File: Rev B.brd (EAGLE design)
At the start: 100.3 x 61 mm, 39 parts

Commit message: Made some changes to the backlight circuit
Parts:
- removed JP_BKL: (no value), pinhead:2X02
- added PRGHDR: (no value), pinhead:1X03
- added Q1: BC817-25LT1SMD, transistor-npn:SOT23-BEC
- added R9: 10kΩ, rcl:R0805
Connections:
- removed net N$11: JP_BKL.3, LCD.15
- new net BKL_CTRL: MCU.4, R9.1
- new net N$16: Q1.B, R9.2
- new net RST: MCU.16, PRGHDR.3, R7.2
- new net TEST: MCU.17, PRGHDR.2
- net +5V: now also LCD.15; no longer JP_BKL.4
- net GND: now also PRGHDR.1, Q1.E; no longer LCD.16
- net N$9: now also LCD.16, Q1.C; no longer MCU.16, R7.2
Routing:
- net BKL_CTRL: track 0.00 -> 52.1 mm, vias 0 -> 1
- net N$11: track 43.9 -> 0.00 mm, vias 1 -> 0
- net RST: track 0.00 -> 43.2 mm
- net TEST: track 0.00 -> 22.4 mm, vias 0 -> 1
- net N$9: track 19.3 -> 38.2 mm, vias 0 -> 1
- net +5V: track 104.1 -> 89.9 mm, vias 5 -> 4
- net N$16: track 0.00 -> 3.64 mm
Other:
- board text removed: "Backlight"
- board text removed: "OFF"

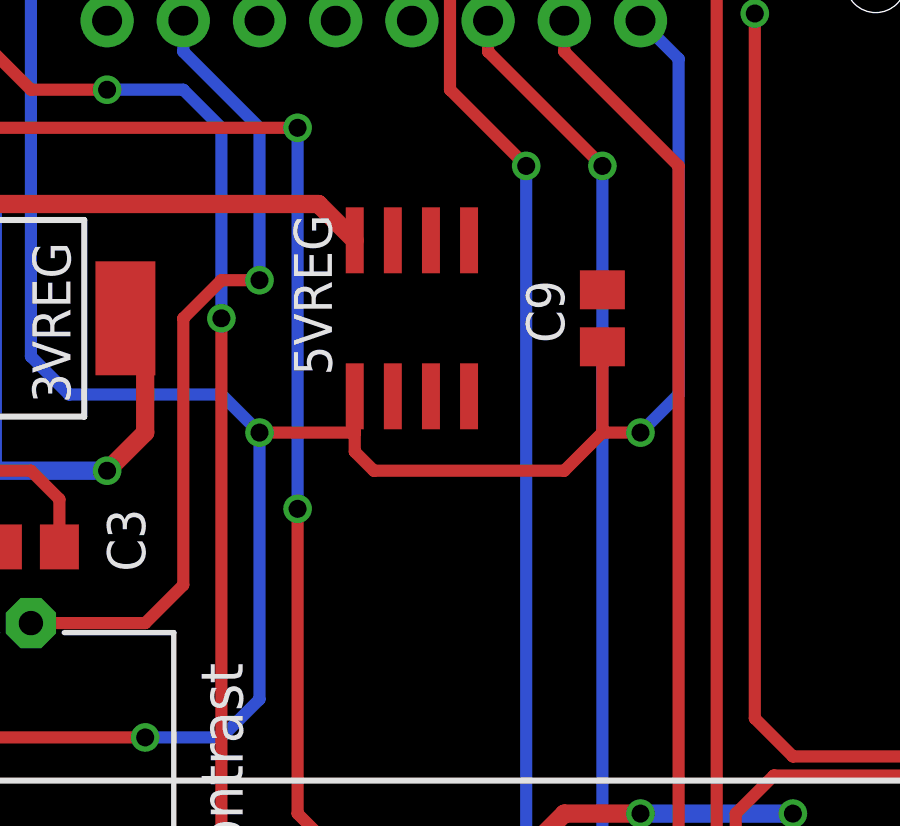
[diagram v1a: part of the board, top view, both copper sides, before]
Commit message: Changed the 5V regulators
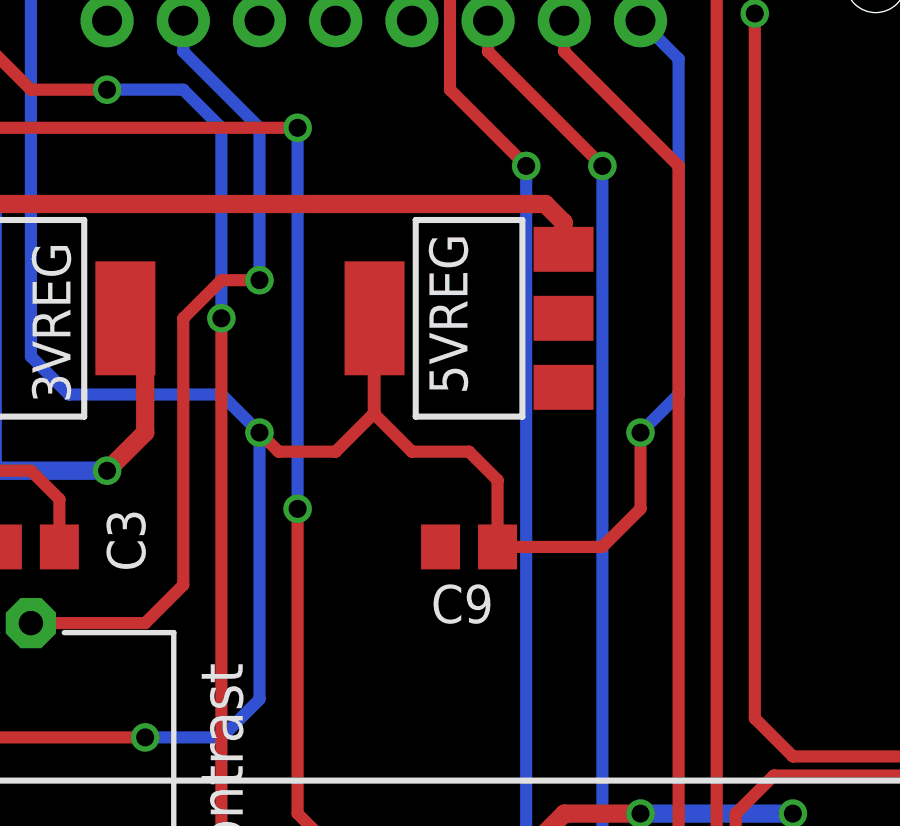
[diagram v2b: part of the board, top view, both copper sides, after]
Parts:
- 5VREG: value 78L05SMD -> LD117AS50TR; device linear:SO08 -> v-reg:SOT223
- moved C9 8.82 mm to (31.1, 38.1), turned to 0 degrees
- moved 5VREG 1.90 mm to (31.1, 45.7), turned to 90 degrees
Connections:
- net +5V: now also 5VREG.4; no longer 5VREG.1
- net GND: now also 5VREG.1; no longer 5VREG.2, 5VREG.3, 5VREG.6, 5VREG.7
- net N$6: now also 5VREG.3; no longer 5VREG.8
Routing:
- net +5V: track 89.9 -> 97.8 mm
- net N$6: track 55.2 -> 62.8 mm
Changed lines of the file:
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@@
 </element>
 <element name="VO" library="bourns" package="3386G" value="10kΩ" x="16.51" y="30.48"/>
-<element name="5VREG" library="linear" package="SO08" value="78L05SMD" x="29.21" y="45.72"/>
-<element name="C9" library="rcl" package="C0805" value="0.1uF" x="35.56" y="45.72" smashed="yes" rot="R270">
-<attribute name="NAME" x="33.02" y="46.99" size="1.27" layer="25" rot="R270"/>
-<attribute name="VALUE" x="33.02" y="46.99" size="1.27" layer="27" rot="R270"/>
+<element name="C9" library="rcl" package="C0805" value="0.1uF" x="31.115" y="38.1" smashed="yes">
+<attribute name="NAME" x="29.845" y="35.56" size="1.27" layer="25"/>
+<attribute name="VALUE" x="29.845" y="35.56" size="1.27" layer="27"/>
 </element>
 <element name="PWR_IN" library="SparkFun-Connectors" package="JST-2-PTH" value="M02JST-PTH-2" x="93.98" y="24.13" rot="R270"/>
@@
 <element name="Q1" library="transistor-npn" package="SOT23-BEC" value="BC817-25LT1SMD" x="50.165" y="31.115" rot="R90"/>
 <element name="R9" library="rcl" package="R0805" value="10kΩ" x="50.165" y="26.035" rot="R90"/>
+<element name="5VREG" library="v-reg" package="SOT223" value="LD117AS50TR" x="31.115" y="45.72" rot="R90"/>
 </elements>
 <signals>
@@
 <contactref element="RE1" pad="SW+"/>
 <contactref element="VO" pad="3"/>
-<contactref element="5VREG" pad="2"/>
-<contactref element="5VREG" pad="7"/>
-<contactref element="5VREG" pad="6"/>
-<contactref element="5VREG" pad="3"/>
 <contactref element="C9" pad="1"/>
 <contactref element="PWR_IN" pad="1"/>
@@
 <contactref element="PRGHDR" pad="1"/>
 <contactref element="Q1" pad="E"/>
+<contactref element="5VREG" pad="1"/>
 <wire x1="90.17" y1="24.13" x2="93.98" y2="25.13" width="0" layer="19" extent="1-1"/>
 <wire x1="90.17" y1="29.21" x2="90.17" y2="24.13" width="0" layer="19" extent="1-1"/>
@@
 <wire x1="48.26" y1="18.1" x2="58.42" y2="6.35" width="0" layer="19" extent="1-1"/>
 <wire x1="43.18" y1="20" x2="48.26" y2="18.1" width="0" layer="19" extent="1-1"/>
-<wire x1="19.05" y1="25.4" x2="43.18" y2="20" width="0" layer="19" extent="1-1"/>
+<wire x1="51.265" y1="32.065" x2="48.26" y2="18.1" width="0" layer="19" extent="1-1"/>
+<wire x1="30.165" y1="38.1" x2="51.265" y2="32.065" width="0" layer="19" extent="1-1"/>
+<wire x1="24.13" y1="55.64" x2="30.165" y2="38.1" width="0" layer="19" extent="1-1"/>
+<wire x1="19.05" y1="55.64" x2="24.13" y2="55.64" width="0" layer="19" extent="1-1"/>
+<wire x1="13.36" y1="48.02" x2="19.05" y2="55.64" width="0" layer="19" extent="1-1"/>
+<wire x1="3.81" y1="45.59" x2="13.36" y2="48.02" width="0" layer="19" extent="1-1"/>
+<wire x1="15.56" y1="38.1" x2="13.36" y2="48.02" width="0" layer="19" extent="1-1"/>
+<wire x1="11.11" y1="38.1" x2="15.56" y2="38.1" width="0" layer="19" extent="1-1"/>
+<wire x1="6.35" y1="56.15" x2="13.36" y2="48.02" width="0" layer="19" extent="1-1"/>
+<wire x1="3.81" y1="27.94" x2="11.11" y2="38.1" width="0" layer="19" extent="1-1"/>
+<wire x1="19.05" y1="25.4" x2="15.56" y2="38.1" width="0" layer="19" extent="1-1"/>
 <wire x1="15.235" y1="20.32" x2="19.05" y2="25.4" width="0" layer="19" extent="1-1"/>
 <wire x1="10.16" y1="13.02" x2="15.235" y2="20.32" width="0" layer="19" extent="1-1"/>
 <wire x1="3.81" y1="11.43" x2="10.16" y2="13.02" width="0" layer="19" extent="1-1"/>
-<wire x1="15.56" y1="38.1" x2="19.05" y2="25.4" width="0" layer="19" extent="1-1"/>
-<wire x1="11.11" y1="38.1" x2="15.56" y2="38.1" width="0" layer="19" extent="1-1"/>
-<wire x1="13.36" y1="48.02" x2="15.56" y2="38.1" width="0" layer="19" extent="1-1"/>
-<wire x1="19.05" y1="55.64" x2="13.36" y2="48.02" width="0" layer="19" extent="1-1"/>
-<wire x1="24.13" y1="55.64" x2="19.05" y2="55.64" width="0" layer="19" extent="1-1"/>
-<wire x1="28.575" y1="48.32" x2="24.13" y2="55.64" width="0" layer="19" extent="1-1"/>
-<wire x1="29.845" y1="48.32" x2="28.575" y2="48.32" width="0" layer="19" extent="1-1"/>
-<wire x1="28.575" y1="43.12" x2="28.575" y2="48.32" width="0" layer="19" extent="1-1"/>
-<wire x1="29.845" y1="43.12" x2="28.575" y2="43.12" width="0" layer="19" extent="1-1"/>
-<wire x1="35.56" y1="46.67" x2="29.845" y2="48.32" width="0" layer="19" extent="1-1"/>
-<wire x1="3.81" y1="45.59" x2="13.36" y2="48.02" width="0" layer="19" extent="1-1"/>
-<wire x1="6.35" y1="56.15" x2="13.36" y2="48.02" width="0" layer="19" extent="1-1"/>
-<wire x1="3.81" y1="27.94" x2="11.11" y2="38.1" width="0" layer="19" extent="1-1"/>
-<wire x1="51.265" y1="32.065" x2="3.81" y2="11.43" width="0" layer="19" extent="1-1"/>
+<wire x1="34.265" y1="43.42" x2="3.81" y2="11.43" width="0" layer="19" extent="1-1"/>
 </signal>
 <signal name="VCC">
@@
 <wire x1="11.43" y1="43.18" x2="13.12" y2="43.18" width="0.6096" layer="1"/>
 <wire x1="13.12" y1="43.18" x2="13.36" y2="43.42" width="0.6096" layer="1"/>
-<contactref element="5VREG" pad="8"/>
 <wire x1="9.16" y1="46.72" x2="9.16" y2="46.99" width="0.6096" layer="1"/>
 <wire x1="9.16" y1="46.99" x2="9.16" y2="48.53" width="0.6096" layer="1"/>
 <wire x1="9.16" y1="48.53" x2="10.16" y2="49.53" width="0.6096" layer="1"/>
 <wire x1="10.16" y1="49.53" x2="26.095" y2="49.53" width="0.6096" layer="1"/>
-<wire x1="26.095" y1="49.53" x2="27.305" y2="48.32" width="0.6096" layer="1"/>
 <wire x1="6.35" y1="58.15" x2="4.81" y2="58.15" width="0.6096" layer="16"/>
 <wire x1="4.81" y1="58.15" x2="2.54" y2="55.88" width="0.6096" layer="16"/>
@@
 <wire x1="9.16" y1="46.99" x2="6.985" y2="46.99" width="0.6096" layer="1"/>
 <via x="6.985" y="46.99" extent="1-16" drill="0.6"/>
+<contactref element="5VREG" pad="3"/>
+<wire x1="34.265" y1="48.02" x2="34.265" y2="48.92" width="0.6096" layer="1"/>
+<wire x1="34.265" y1="48.92" x2="33.655" y2="49.53" width="0.6096" layer="1"/>
+<wire x1="33.655" y1="49.53" x2="26.095" y2="49.53" width="0.6096" layer="1"/>
 </signal>
 <signal name="N$7">
@@
 </signal>
 <signal name="+5V">
-<contactref element="5VREG" pad="1"/>
 <contactref element="VO" pad="1"/>
 <contactref element="LCD" pad="2"/>
 <contactref element="C9" pad="2"/>
-<wire x1="27.94" y1="40.64" x2="27.305" y2="41.275" width="0.4064" layer="1"/>
-<wire x1="27.305" y1="41.275" x2="27.305" y2="41.91" width="0.4064" layer="1"/>
-<wire x1="27.305" y1="41.91" x2="27.305" y2="43.12" width="0.4064" layer="1"/>
-<wire x1="27.94" y1="40.64" x2="34.29" y2="40.64" width="0.4064" layer="1"/>
-<wire x1="34.29" y1="40.64" x2="35.56" y2="41.91" width="0.4064" layer="1"/>
-<wire x1="35.56" y1="41.91" x2="35.56" y2="44.77" width="0.4064" layer="1"/>
 <wire x1="19.05" y1="58.18" x2="17.54" y2="58.18" width="0.4064" layer="1"/>
 <wire x1="17.54" y1="58.18" x2="16.51" y2="57.15" width="0.4064" layer="1"/>
@@
 <wire x1="22.86" y1="43.18" x2="24.13" y2="41.91" width="0.4064" layer="16"/>
 <via x="24.13" y="41.91" extent="1-16" drill="0.6"/>
-<wire x1="24.13" y1="41.91" x2="27.305" y2="41.91" width="0.4064" layer="1"/>
 <via x="36.83" y="41.91" extent="1-16" drill="0.6"/>
-<wire x1="36.83" y1="41.91" x2="35.56" y2="41.91" width="0.4064" layer="1"/>
 <wire x1="13.97" y1="25.4" x2="13.97" y2="30.48" width="0.4064" layer="1"/>
 <wire x1="13.97" y1="30.48" x2="15.24" y2="31.75" width="0.4064" layer="1"/>
@@
 <wire x1="38.1" y1="43.18" x2="38.1" y2="54.37" width="0.4064" layer="16"/>
 <wire x1="38.1" y1="54.37" x2="36.83" y2="55.64" width="0.4064" layer="16"/>
+<contactref element="5VREG" pad="4"/>
+<wire x1="36.83" y1="41.91" x2="36.83" y2="39.37" width="0.4064" layer="1"/>
+<wire x1="36.83" y1="39.37" x2="35.56" y2="38.1" width="0.4064" layer="1"/>
+<wire x1="35.56" y1="38.1" x2="32.065" y2="38.1" width="0.4064" layer="1"/>
+<wire x1="32.065" y1="38.1" x2="32.065" y2="40.325" width="0.4064" layer="1"/>
+<wire x1="32.065" y1="40.325" x2="31.115" y2="41.275" width="0.4064" layer="1"/>
+<wire x1="31.115" y1="41.275" x2="29.21" y2="41.275" width="0.4064" layer="1"/>
+<wire x1="29.21" y1="41.275" x2="27.94" y2="42.545" width="0.4064" layer="1"/>
+<wire x1="27.94" y1="42.545" x2="27.94" y2="45.695" width="0.4064" layer="1"/>
+<wire x1="27.94" y1="45.695" x2="27.965" y2="45.72" width="0.4064" layer="1"/>
+<wire x1="27.965" y1="45.72" x2="27.965" y2="42.57" width="0.4064" layer="1"/>
+<wire x1="27.965" y1="42.57" x2="26.67" y2="41.275" width="0.4064" layer="1"/>
+<wire x1="26.67" y1="41.275" x2="24.765" y2="41.275" width="0.4064" layer="1"/>
+<wire x1="24.765" y1="41.275" x2="24.13" y2="41.91" width="0.4064" layer="1"/>
 </signal>
 <signal name="N$2">

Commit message: Final design
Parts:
- removed VO: 10kΩ, bourns:3386G
- added R10: TRIMPOT-2, SparkFun-Electromechanical:TRIMPOT_TC33
- moved 5V 1.27 mm to (7.62, 21.6)
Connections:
- net +5V: now also R10.1; no longer VO.1
- net GND: now also R10.3; no longer VO.3
- net N$10: now also R10.2; no longer VO.2
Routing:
- net N$10: track 27.3 -> 33.6 mm
- net +5V: track 97.8 -> 103.7 mm
- net BKL_CTRL: track 52.1 -> 53.1 mm
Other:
- board text added: "Rev B"
- board text removed: "Contrast"
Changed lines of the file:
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@@
 <text x="3.81" y="40.64" size="1.6764" layer="21" font="vector" align="center">ON</text>
 <text x="74.93" y="38.1" size="1.6764" layer="21" font="vector" align="center">MOSFET</text>
-<text x="22.86" y="30.48" size="1.4224" layer="21" rot="R90" align="center">Contrast</text>
 <text x="96.52" y="29.21" size="1.9304" layer="21" align="center">Input</text>
 <text x="24.13" y="7.62" size="3.81" layer="21" align="center">miniLoad</text>
@@
 <rectangle x1="53.34" y1="59.69" x2="96.52" y2="60.96" layer="41"/>
 <text x="3.81" y="52.705" size="1.778" layer="21" align="center">PWR</text>
-<wire x1="2.54" y1="8.89" x2="5.08" y2="8.89" width="0.4064" layer="21"/>
-<wire x1="5.08" y1="8.89" x2="5.08" y2="10.16" width="0.4064" layer="21"/>
-<wire x1="2.54" y1="8.89" x2="2.54" y2="10.16" width="0.4064" layer="21"/>
+<wire x1="5.08" y1="10.16" x2="6.35" y2="10.16" width="0.4064" layer="21"/>
+<wire x1="6.35" y1="10.16" x2="6.35" y2="12.7" width="0.4064" layer="21"/>
+<wire x1="6.35" y1="12.7" x2="5.08" y2="12.7" width="0.4064" layer="21"/>
+<wire x1="2.54" y1="18.415" x2="5.08" y2="18.415" width="0.4064" layer="21"/>
+<wire x1="2.54" y1="19.05" x2="5.08" y2="19.05" width="0.4064" layer="21"/>
+<text x="5.08" y="1.905" size="1.27" layer="21" align="center">Rev B</text>
 </plain>
 <attributes>
@@
 <attribute name="VALUE" x="80.01" y="17.145" size="1.27" layer="27" rot="R270"/>
 </element>
-<element name="VO" library="bourns" package="3386G" value="10kΩ" x="16.51" y="30.48"/>
 <element name="C9" library="rcl" package="C0805" value="0.1uF" x="31.115" y="38.1" smashed="yes">
 <attribute name="NAME" x="29.845" y="35.56" size="1.27" layer="25"/>
@@
 <attribute name="TP_SIGNAL_NAME" value="" x="7.62" y="15.24" size="1.27" layer="27" rot="R90" display="off"/>
 </element>
-<element name="5V" library="testpad" package="TP10SQ" value="PTR1TP10SQ" x="7.62" y="22.86" rot="R90">
-<attribute name="TP_SIGNAL_NAME" value="" x="7.62" y="22.86" size="1.27" layer="27" rot="R90" display="off"/>
+<element name="5V" library="testpad" package="TP10SQ" value="PTR1TP10SQ" x="7.62" y="21.59" rot="R90">
+<attribute name="TP_SIGNAL_NAME" value="" x="7.62" y="21.59" size="1.27" layer="27" rot="R90" display="off"/>
 </element>
 <element name="GND" library="testpad" package="TP10SQ" value="PTR1TP10SQ" x="3.81" y="27.94" rot="R90">
@@
 <element name="R9" library="rcl" package="R0805" value="10kΩ" x="50.165" y="26.035" rot="R90"/>
 <element name="5VREG" library="v-reg" package="SOT223" value="LD117AS50TR" x="31.115" y="45.72" rot="R90"/>
+<element name="R10" library="SparkFun-Electromechanical" package="TRIMPOT_TC33" value="TRIMPOT-2" x="13.335" y="29.845"/>
 </elements>
 <signals>
@@
 <contactref element="OP2" pad="4"/>
 <contactref element="RE1" pad="SW+"/>
-<contactref element="VO" pad="3"/>
 <contactref element="C9" pad="1"/>
 <contactref element="PWR_IN" pad="1"/>
@@
 <contactref element="Q1" pad="E"/>
 <contactref element="5VREG" pad="1"/>
-<wire x1="90.17" y1="24.13" x2="93.98" y2="25.13" width="0" layer="19" extent="1-1"/>
-<wire x1="90.17" y1="29.21" x2="90.17" y2="24.13" width="0" layer="19" extent="1-1"/>
-<wire x1="93.98" y1="17.145" x2="90.17" y2="24.13" width="0" layer="19" extent="1-1"/>
-<wire x1="91.44" y1="2.667" x2="93.98" y2="17.145" width="0" layer="19" extent="1-1"/>
-<wire x1="80.01" y1="9.21" x2="91.44" y2="2.667" width="0" layer="19" extent="1-1"/>
-<wire x1="74.93" y1="6.35" x2="80.01" y2="9.21" width="0" layer="19" extent="1-1"/>
-<wire x1="58.42" y1="6.35" x2="74.93" y2="6.35" width="0" layer="19" extent="1-1"/>
-<wire x1="48.26" y1="18.1" x2="58.42" y2="6.35" width="0" layer="19" extent="1-1"/>
-<wire x1="43.18" y1="20" x2="48.26" y2="18.1" width="0" layer="19" extent="1-1"/>
-<wire x1="51.265" y1="32.065" x2="48.26" y2="18.1" width="0" layer="19" extent="1-1"/>
-<wire x1="30.165" y1="38.1" x2="51.265" y2="32.065" width="0" layer="19" extent="1-1"/>
-<wire x1="24.13" y1="55.64" x2="30.165" y2="38.1" width="0" layer="19" extent="1-1"/>
-<wire x1="19.05" y1="55.64" x2="24.13" y2="55.64" width="0" layer="19" extent="1-1"/>
-<wire x1="13.36" y1="48.02" x2="19.05" y2="55.64" width="0" layer="19" extent="1-1"/>
-<wire x1="3.81" y1="45.59" x2="13.36" y2="48.02" width="0" layer="19" extent="1-1"/>
-<wire x1="15.56" y1="38.1" x2="13.36" y2="48.02" width="0" layer="19" extent="1-1"/>
-<wire x1="11.11" y1="38.1" x2="15.56" y2="38.1" width="0" layer="19" extent="1-1"/>
-<wire x1="6.35" y1="56.15" x2="13.36" y2="48.02" width="0" layer="19" extent="1-1"/>
-<wire x1="3.81" y1="27.94" x2="11.11" y2="38.1" width="0" layer="19" extent="1-1"/>
-<wire x1="19.05" y1="25.4" x2="15.56" y2="38.1" width="0" layer="19" extent="1-1"/>
-<wire x1="15.235" y1="20.32" x2="19.05" y2="25.4" width="0" layer="19" extent="1-1"/>
-<wire x1="10.16" y1="13.02" x2="15.235" y2="20.32" width="0" layer="19" extent="1-1"/>
-<wire x1="3.81" y1="11.43" x2="10.16" y2="13.02" width="0" layer="19" extent="1-1"/>
-<wire x1="34.265" y1="43.42" x2="3.81" y2="11.43" width="0" layer="19" extent="1-1"/>
+<contactref element="R10" pad="3"/>
+<via x="10.795" y="47.625" extent="1-16" drill="0.6"/>
+<via x="29.21" y="33.02" extent="1-16" drill="0.6"/>
+<via x="34.29" y="40.64" extent="1-16" drill="0.6"/>
 </signal>
 <signal name="VCC">
@@
 <signal name="N$10">
 <contactref element="LCD" pad="3"/>
-<contactref element="VO" pad="2"/>
-<wire x1="16.51" y1="35.56" x2="20.32" y2="35.56" width="0.4064" layer="1"/>
 <wire x1="20.32" y1="35.56" x2="21.59" y2="36.83" width="0.4064" layer="1"/>
 <wire x1="21.59" y1="36.83" x2="21.59" y2="45.72" width="0.4064" layer="1"/>
@@
 <wire x1="24.13" y1="52.07" x2="21.59" y2="54.61" width="0.4064" layer="16"/>
 <wire x1="21.59" y1="54.61" x2="21.59" y2="55.64" width="0.4064" layer="16"/>
+<contactref element="R10" pad="2"/>
+<wire x1="13.335" y1="31.295" x2="13.335" y2="33.655" width="0.4064" layer="1"/>
+<wire x1="13.335" y1="33.655" x2="15.24" y2="35.56" width="0.4064" layer="1"/>
+<wire x1="15.24" y1="35.56" x2="20.32" y2="35.56" width="0.4064" layer="1"/>
 </signal>
 <signal name="RS">
@@
 </signal>
 <signal name="+5V">
-<contactref element="VO" pad="1"/>
 <contactref element="LCD" pad="2"/>
 <contactref element="C9" pad="2"/>
@@
 <via x="24.13" y="41.91" extent="1-16" drill="0.6"/>
 <via x="36.83" y="41.91" extent="1-16" drill="0.6"/>
-<wire x1="13.97" y1="25.4" x2="13.97" y2="30.48" width="0.4064" layer="1"/>
-<wire x1="13.97" y1="30.48" x2="15.24" y2="31.75" width="0.4064" layer="1"/>
-<wire x1="15.24" y1="31.75" x2="20.32" y2="31.75" width="0.4064" layer="1"/>
 <via x="20.32" y="31.75" extent="1-16" drill="0.6"/>
 <wire x1="20.32" y1="31.75" x2="22.86" y2="31.75" width="0.4064" layer="16"/>
@@
 <wire x1="24.13" y1="33.02" x2="24.13" y2="41.91" width="0.4064" layer="16"/>
 <contactref element="5V" pad="TP"/>
-<wire x1="7.62" y1="22.86" x2="10.16" y2="22.86" width="0.4064" layer="1"/>
-<wire x1="10.16" y1="22.86" x2="12.7" y2="25.4" width="0.4064" layer="1"/>
-<wire x1="12.7" y1="25.4" x2="13.97" y2="25.4" width="0.4064" layer="1"/>
 <wire x1="36.83" y1="41.91" x2="38.1" y2="43.18" width="0.4064" layer="16"/>
 <contactref element="LCD" pad="15"/>
@@
 <wire x1="26.67" y1="41.275" x2="24.765" y2="41.275" width="0.4064" layer="1"/>
 <wire x1="24.765" y1="41.275" x2="24.13" y2="41.91" width="0.4064" layer="1"/>
+<contactref element="R10" pad="1"/>
+<wire x1="20.32" y1="25.4" x2="20.32" y2="31.75" width="0.4064" layer="1"/>
+<wire x1="20.32" y1="25.4" x2="19.05" y2="24.13" width="0.4064" layer="1"/>
+<wire x1="19.05" y1="24.13" x2="11.43" y2="24.13" width="0.4064" layer="1"/>
+<wire x1="11.43" y1="24.13" x2="8.89" y2="21.59" width="0.4064" layer="1"/>
+<wire x1="8.89" y1="21.59" x2="7.62" y2="21.59" width="0.4064" layer="1"/>
+<wire x1="12.425" y1="28.395" x2="12.425" y2="26.395" width="0.4064" layer="1"/>
+<wire x1="12.425" y1="26.395" x2="11.43" y2="25.4" width="0.4064" layer="1"/>
+<wire x1="11.43" y1="25.4" x2="11.43" y2="24.13" width="0.4064" layer="1"/>
 </signal>
 <signal name="N$2">
@@
 <wire x1="22.86" y1="11.43" x2="22.86" y2="12.695" width="0.4064" layer="16"/>
 <wire x1="22.86" y1="12.695" x2="22.855" y2="12.7" width="0.4064" layer="16"/>
-<wire x1="49.215" y1="25.085" x2="48.575" y2="25.085" width="0.4064" layer="1"/>
 <wire x1="48.575" y1="25.085" x2="47.625" y2="26.035" width="0.4064" layer="1"/>
 <wire x1="47.625" y1="26.035" x2="47.625" y2="29.21" width="0.4064" layer="1"/>
@@
 <wire x1="41.275" y1="30.48" x2="40.005" y2="29.21" width="0.4064" layer="1"/>
 <wire x1="40.005" y1="29.21" x2="40.005" y2="24.765" width="0.4064" layer="1"/>
-<wire x1="49.215" y1="25.085" x2="50.165" y2="25.085" width="0" layer="19" extent="1-1"/>
+<wire x1="48.575" y1="25.085" x2="50.165" y2="25.085" width="0.4064" layer="1"/>
 </signal>
 </signals>
